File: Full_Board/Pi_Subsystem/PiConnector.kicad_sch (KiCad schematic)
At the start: 5 parts, among them J1 USB_A, U2 UCLAMP3301H.TCT, U3 UCLAMP3301H.TCT

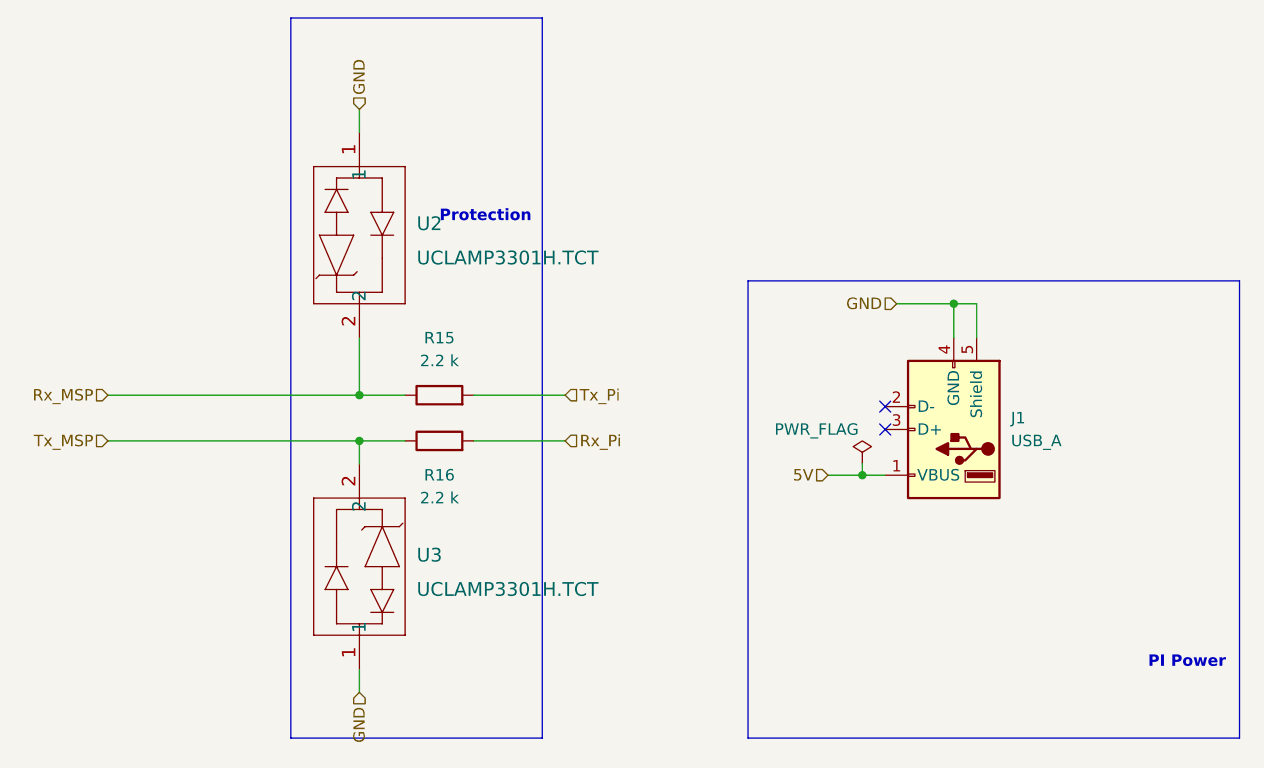
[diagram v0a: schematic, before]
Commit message: Redo pinout, finish pcb layout (no traces)
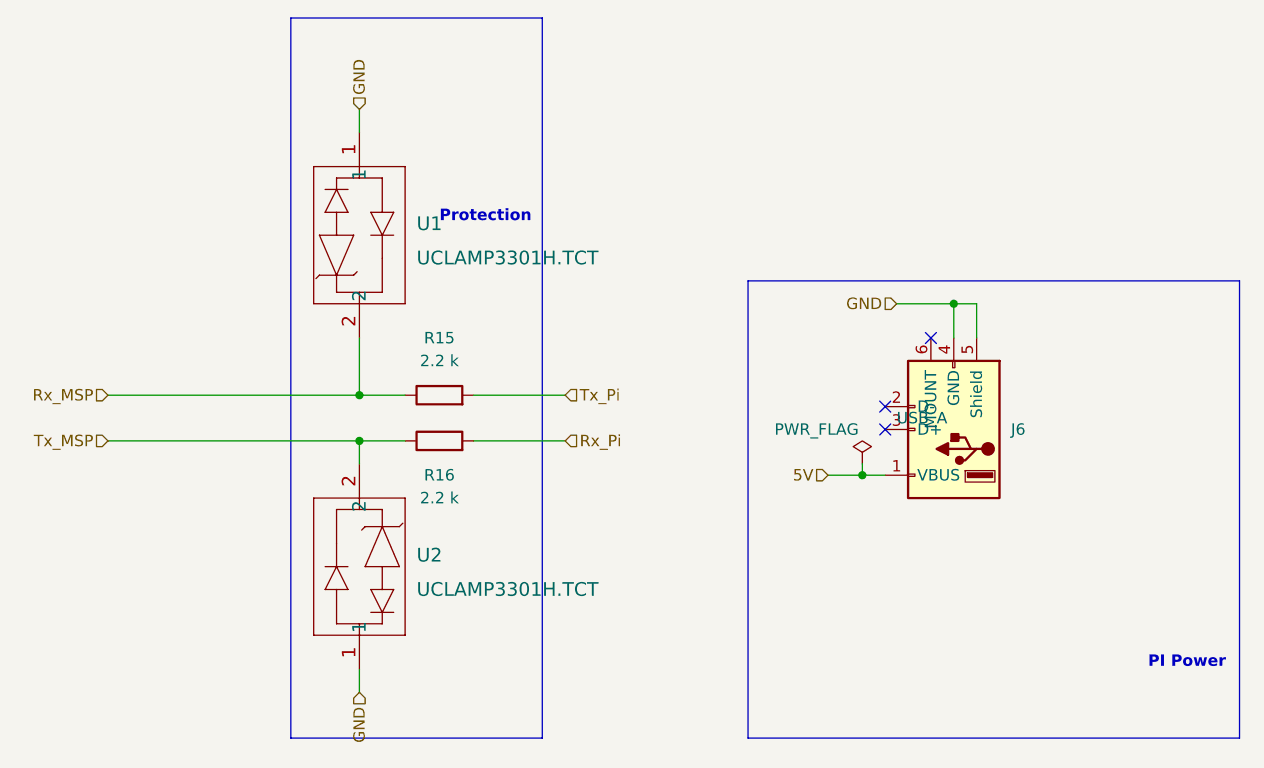
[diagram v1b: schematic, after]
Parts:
- renumbered J1 to J6, U2 to U1, U3 to U2
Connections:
- no-connect marks 2 -> 3
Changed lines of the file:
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@@
   )
   (no_connect (at 213.36 99.06))
+  (no_connect (at 218.44 91.44))
   (no_connect (at 213.36 101.6))
   (wire (pts (xy 154.94 97.79) (xy 160.02 97.79))
@@
   )
   (symbol (lib_id "Connector:USB_A") (at 220.98 101.6 180) (unit 1)
-    (in_bom yes) (on_board yes) (fields_autoplaced)
-    (property "Reference" "J1" (id 0) (at 227.33 100.3299 0)
+    (in_bom yes) (on_board yes)
+    (property "Reference" "J6" (id 0) (at 227.33 101.6 0)
       (effects (font (size 1.27 1.27)) (justify right))
     )
-    (property "Value" "USB_A" (id 1) (at 227.33 102.8699 0)
+    (property "Value" "USB_A" (id 1) (at 214.63 100.3301 0)
       (effects (font (size 1.27 1.27)) (justify right))
     )
-    (property "Footprint" "USB1130-15-A:USB1130-15-A" (id 2) (at 217.17 100.33 0)
-      (effects (font (size 1.27 1.27)) hide)
-    )
-    (property "Datasheet" "https://media.digikey.com/pdf/Data%20Sheets/GCT%20PDFs/USB1130-USB1135.pdf" (id 3) (at 217.17 100.33 0)
+    (property "Footprint" "USB1130-15-A:USB1130-15-A" (id 2) (at 224.79 102.87 0)
+      (effects (font (size 1.27 1.27)) hide)
+    )
+    (property "Datasheet" " ~" (id 3) (at 224.79 102.87 0)
       (effects (font (size 1.27 1.27)) hide)
     )
@@
     (pin "3")
     (pin "4")
+    (pin "6")
     (pin "5")
   )
   (symbol (lib_id "UCLAMP3301H-TCT:UCLAMP3301H.TCT") (at 154.94 59.69 270) (unit 1)
     (in_bom yes) (on_board yes) (fields_autoplaced)
-    (property "Reference" "U2" (id 0) (at 161.29 78.74 90)
+    (property "Reference" "U1" (id 0) (at 161.29 78.74 90)
       (effects (font (size 1.524 1.524)) (justify left))
     )
@@
     (pin "2")
   )
-  (symbol (lib_name "UCLAMP3301H.TCT_2") (lib_id "UCLAMP3301H-TCT:UCLAMP3301H.TCT") (at 154.94 137.16 90) (unit 1)
+  (symbol (lib_id "UCLAMP3301H-TCT:UCLAMP3301H.TCT") (at 154.94 137.16 90) (unit 1)
     (in_bom yes) (on_board yes) (fields_autoplaced)
-    (property "Reference" "U3" (id 0) (at 161.29 115.57 90)
+    (property "Reference" "U2" (id 0) (at 161.29 115.57 90)
       (effects (font (size 1.524 1.524)) (justify right))
     )
@@
   (symbol (lib_id "power:PWR_FLAG") (at 210.82 105.41 0) (unit 1)
     (in_bom yes) (on_board yes)
-    (property "Reference" "#FLG0101" (id 0) (at 210.82 103.505 0)
-      (effects (font (size 1.27 1.27)) hide)
-    )
+    (property "Reference" "#FLG01" (id 0) (at 210.82 103.505 0)
+      (effects (font (size 1.27 1.27)) hide)
+    )

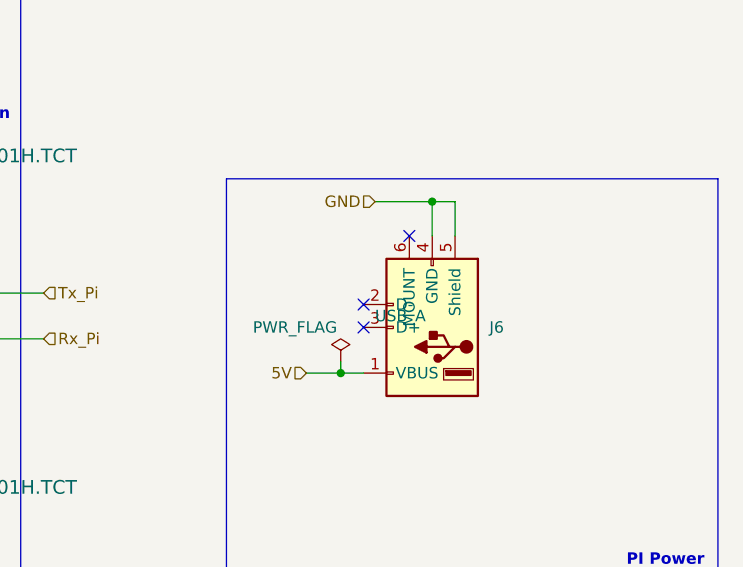
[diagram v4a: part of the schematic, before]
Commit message: Swapped resistors in stepper driver
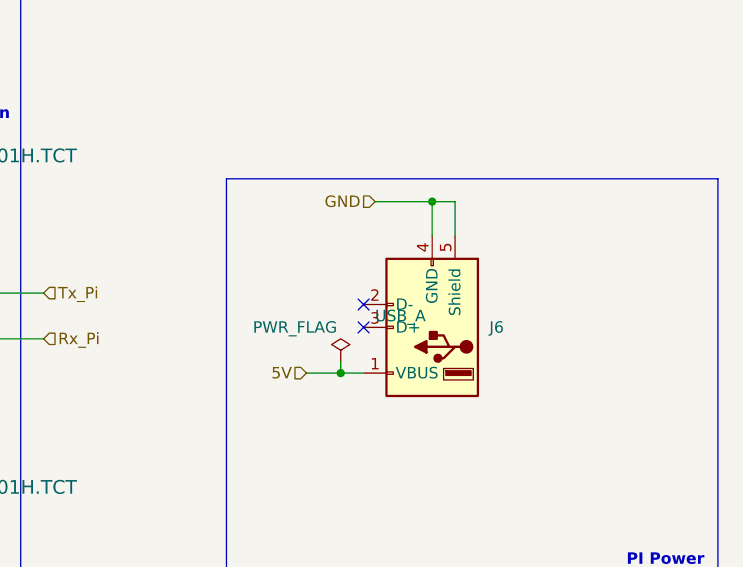
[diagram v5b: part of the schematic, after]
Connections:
- no-connect marks 3 -> 2
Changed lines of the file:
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@@
   )
   (no_connect (at 213.36 99.06))
-  (no_connect (at 218.44 91.44))
   (no_connect (at 213.36 101.6))
   (wire (pts (xy 154.94 97.79) (xy 160.02 97.79))
@@
     (pin "4")
     (pin "5")
-    (pin "6")
   )
   (symbol (lib_id "UCLAMP3301H-TCT:UCLAMP3301H.TCT") (at 154.94 59.69 270) (unit 1)

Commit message: Changed Pi resistors back to through hole
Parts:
- R15, R16: Digikey Part Number 511-SDR03EZPF2201CT-ND -> CF14JT2K20CT-ND; Digikey link https://www.digikey.com/en/products/detail/rohm-semiconduct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 -> https://www.digikey.com/en/products/detail/stackpole-electr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; Manufacturer's Part Number SDR03EZPF2201 -> CF14JT2K20; Mouser Part Number 755-SDR03EZPF2201 -> (none); Mouser link https://www.mouser.com/ProductDetail/ROHM-Semiconductor/SDR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 -> (none)
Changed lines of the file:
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@@
       (effects (font (size 1.27 1.27)) hide)
     )
-    (property "Datasheet" "~" (id 3) (at 163.83 97.79 0)
+    (property "Datasheet" "https://www.seielect.com/catalog/sei-cf_cfm.pdf" (id 3) (at 163.83 97.79 0)
       (effects (font (size 1.27 1.27)) hide)
     )
-    (property "Digikey Part Number" "511-SDR03EZPF2201CT-ND" (id 4) (at 163.83 97.79 0)
+    (property "Manufacturer's Part Number" "CF14JT2K20" (id 6) (at 163.83 97.79 0)
       (effects (font (size 1.27 1.27)) hide)
     )
-    (property "Digikey link" "https://www.digikey.com/en/products/detail/rohm-semiconductor/SDR03EZPF2201/16179917?s=N4IgTCBcDaIMoBEBKAGAzAUQFoAUBiYYKAjAAQgC6AvkA" (id 5) (at 163.83 97.79 0)
+    (property "Digikey Part Number" "CF14JT2K20CT-ND" (id 4) (at 163.83 97.79 0)
       (effects (font (size 1.27 1.27)) hide)
     )
-    (property "Manufacturer's Part Number" "SDR03EZPF2201" (id 6) (at 163.83 97.79 0)
+    (property "Mouser Part Number" "" (id 7) (at 163.83 97.79 0)
       (effects (font (size 1.27 1.27)) hide)
     )
-    (property "Mouser Part Number" "755-SDR03EZPF2201" (id 7) (at 163.83 97.79 0)
+    (property "Digikey link" "https://www.digikey.com/en/products/detail/stackpole-electronics-inc/CF14JT2K20/1741321" (id 5) (at 163.83 97.79 0)
       (effects (font (size 1.27 1.27)) hide)
     )
-    (property "Mouser link" "https://www.mouser.com/ProductDetail/ROHM-Semiconductor/SDR03EZPF2201?qs=MyNHzdoqoQJyGuWRlENv2A%3D%3D" (id 8) (at 163.83 97.79 0)
+    (property "Mouser link" "" (id 8) (at 163.83 97.79 0)
       (effects (font (size 1.27 1.27)) hide)
     )
@@
       (effects (font (size 1.27 1.27)) hide)
     )
-    (property "Datasheet" "~" (id 3) (at 163.83 102.87 0)
+    (property "Datasheet" "https://www.seielect.com/catalog/sei-cf_cfm.pdf" (id 3) (at 163.83 102.87 0)
       (effects (font (size 1.27 1.27)) hide)
     )
-    (property "Digikey Part Number" "511-SDR03EZPF2201CT-ND" (id 4) (at 163.83 102.87 0)
+    (property "Manufacturer's Part Number" "CF14JT2K20" (id 6) (at 163.83 102.87 0)
       (effects (font (size 1.27 1.27)) hide)
     )
-    (property "Digikey link" "https://www.digikey.com/en/products/detail/rohm-semiconductor/SDR03EZPF2201/16179917?s=N4IgTCBcDaIMoBEBKAGAzAUQFoAUBiYYKAjAAQgC6AvkA" (id 5) (at 163.83 102.87 0)
+    (property "Digikey Part Number" "CF14JT2K20CT-ND" (id 4) (at 163.83 102.87 0)
       (effects (font (size 1.27 1.27)) hide)
     )
-    (property "Manufacturer's Part Number" "SDR03EZPF2201" (id 6) (at 163.83 102.87 0)
+    (property "Mouser Part Number" "" (id 7) (at 163.83 102.87 0)
       (effects (font (size 1.27 1.27)) hide)
     )
-    (property "Mouser Part Number" "755-SDR03EZPF2201" (id 7) (at 163.83 102.87 0)
+    (property "Digikey link" "https://www.digikey.com/en/products/detail/stackpole-electronics-inc/CF14JT2K20/1741321" (id 5) (at 163.83 102.87 0)
       (effects (font (size 1.27 1.27)) hide)
     )
-    (property "Mouser link" "https://www.mouser.com/ProductDetail/ROHM-Semiconductor/SDR03EZPF2201?qs=MyNHzdoqoQJyGuWRlENv2A%3D%3D" (id 8) (at 163.83 102.87 0)
+    (property "Mouser link" "" (id 8) (at 163.83 102.87 0)
       (effects (font (size 1.27 1.27)) hide)
     )

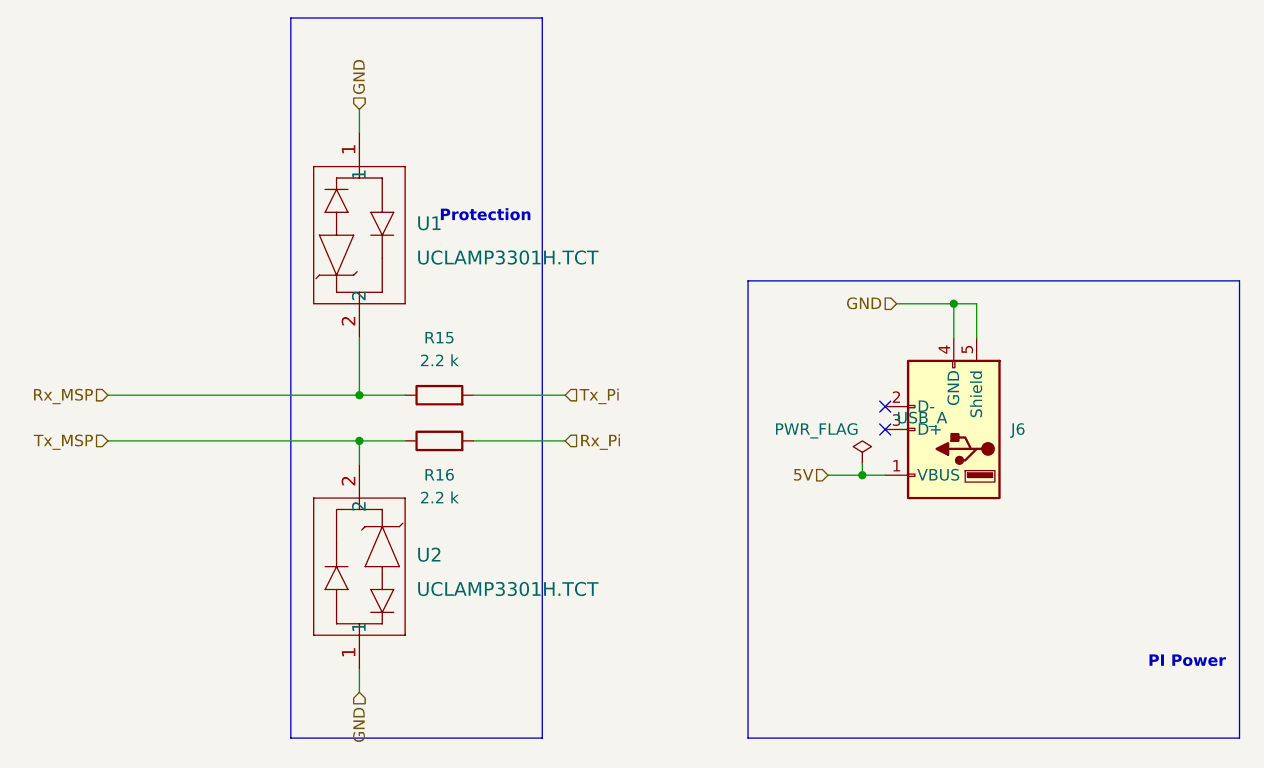
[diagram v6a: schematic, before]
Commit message: Replace small resistors/capacitors with through-hole; fix DRC aside from electromagnet and MUXes
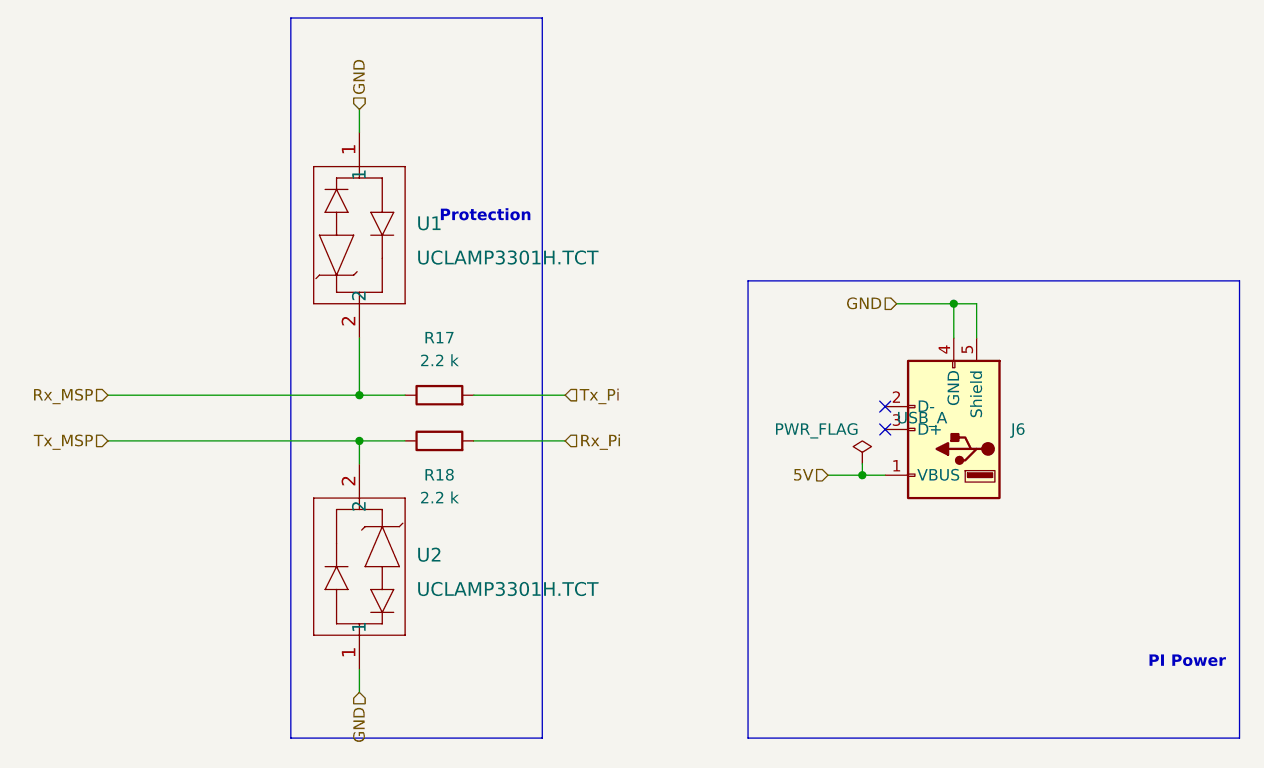
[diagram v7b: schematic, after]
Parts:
- renumbered R15 to R17, R16 to R18
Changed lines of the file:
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@@
   (symbol (lib_id "Device:R") (at 163.83 97.79 90) (unit 1)
     (in_bom yes) (on_board yes) (fields_autoplaced)
-    (property "Reference" "R15" (id 0) (at 163.83 91.44 90))
+    (property "Reference" "R17" (id 0) (at 163.83 91.44 90))
     (property "Value" "2.2 k" (id 1) (at 163.83 93.98 90))
     (property "Footprint" "Resistor_THT:R_Axial_DIN0207_L6.3mm_D2.5mm_P10.16mm_Horizontal" (id 2) (at 163.83 99.568 90)
@@
   (symbol (lib_id "Device:R") (at 163.83 102.87 90) (unit 1)
     (in_bom yes) (on_board yes)
-    (property "Reference" "R16" (id 0) (at 163.83 106.68 90))
+    (property "Reference" "R18" (id 0) (at 163.83 106.68 90))
     (property "Value" "2.2 k" (id 1) (at 163.83 109.22 90))
     (property "Footprint" "Resistor_THT:R_Axial_DIN0207_L6.3mm_D2.5mm_P10.16mm_Horizontal" (id 2) (at 163.83 104.648 90)

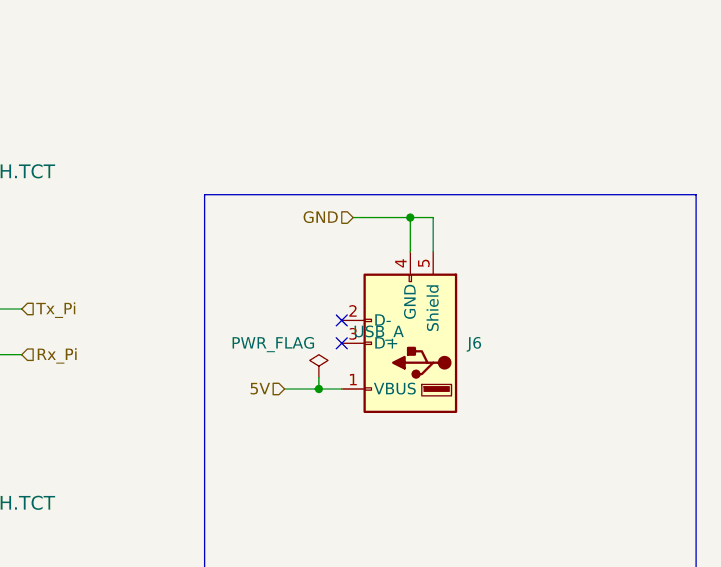
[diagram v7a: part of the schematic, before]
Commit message: Added traces for emag and increased the width of some power lines
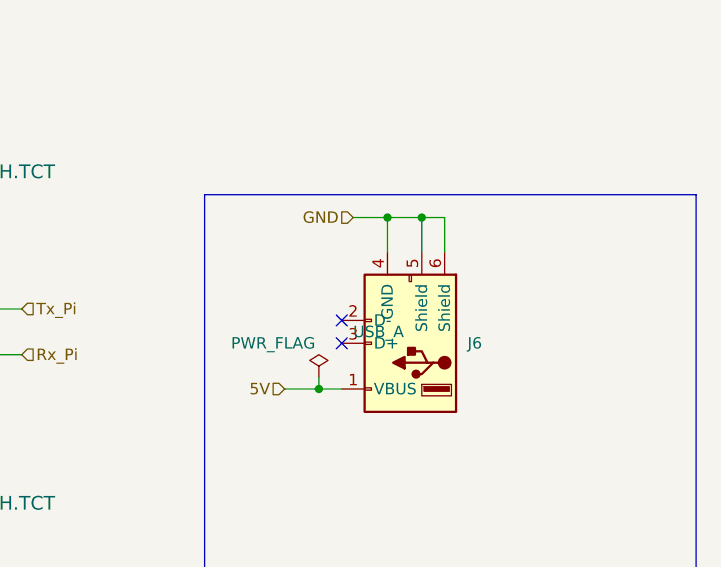
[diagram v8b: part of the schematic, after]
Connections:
- net GND: now also J6.6 (Shield)
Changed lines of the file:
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@@
   (junction (at 154.94 102.87) (diameter 0) (color 0 0 0 0)
   )
-  (junction (at 220.98 87.63) (diameter 0) (color 0 0 0 0)
+  (junction (at 218.44 87.63) (diameter 0) (color 0 0 0 0)
+  )
+  (junction (at 222.25 87.63) (diameter 0) (color 0 0 0 0)
   )
   (junction (at 210.82 106.68) (diameter 0) (color 0 0 0 0)
@@
     (stroke (width 0) (type default) (color 0 0 0 0))
   )
-  (wire (pts (xy 223.52 87.63) (xy 220.98 87.63))
+  (wire (pts (xy 214.63 87.63) (xy 218.44 87.63))
+    (stroke (width 0) (type default) (color 0 0 0 0))
+  )
+  (wire (pts (xy 218.44 87.63) (xy 218.44 91.44))
     (stroke (width 0) (type default) (color 0 0 0 0))
   )
@@
     (stroke (width 0) (type default) (color 0 0 0 0))
   )
+  (wire (pts (xy 218.44 87.63) (xy 222.25 87.63))
+    (stroke (width 0) (type default) (color 0 0 0 0))
+  )
   (wire (pts (xy 210.82 105.41) (xy 210.82 106.68))
     (stroke (width 0) (type default) (color 0 0 0 0))
   )
   (wire (pts (xy 167.64 97.79) (xy 177.8 97.79))
+    (stroke (width 0) (type default) (color 0 0 0 0))
+  )
+  (wire (pts (xy 222.25 87.63) (xy 222.25 91.44))
     (stroke (width 0) (type default) (color 0 0 0 0))
   )
@@
     (stroke (width 0) (type default) (color 0 0 0 0))
   )
-  (wire (pts (xy 220.98 91.44) (xy 220.98 87.63))
+  (wire (pts (xy 224.79 91.44) (xy 224.79 87.63))
     (stroke (width 0) (type default) (color 0 0 0 0))
   )
@@
     (stroke (width 0) (type default) (color 0 0 0 0))
   )
-  (wire (pts (xy 223.52 91.44) (xy 223.52 87.63))
-    (stroke (width 0) (type default) (color 0 0 0 0))
-  )
   (polyline (pts (xy 175.26 55.88) (xy 175.26 135.89))
     (stroke (width 0) (type default) (color 0 0 0 0))
@@
     (stroke (width 0) (type default) (color 0 0 0 0))
   )
+  (wire (pts (xy 222.25 87.63) (xy 224.79 87.63))
+    (stroke (width 0) (type default) (color 0 0 0 0))
+  )
   (polyline (pts (xy 252.73 135.89) (xy 198.12 135.89))
     (stroke (width 0) (type default) (color 0 0 0 0))
   )
   (wire (pts (xy 167.64 102.87) (xy 177.8 102.87))
-    (stroke (width 0) (type default) (color 0 0 0 0))
-  )
-  (wire (pts (xy 214.63 87.63) (xy 220.98 87.63))
     (stroke (width 0) (type default) (color 0 0 0 0))
   )
@@
     (pin "4")
     (pin "5")
+    (pin "6")
   )
   (symbol (lib_id "UCLAMP3301H-TCT:UCLAMP3301H.TCT") (at 154.94 59.69 270) (unit 1)
